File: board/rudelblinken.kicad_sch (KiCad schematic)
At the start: 0 parts

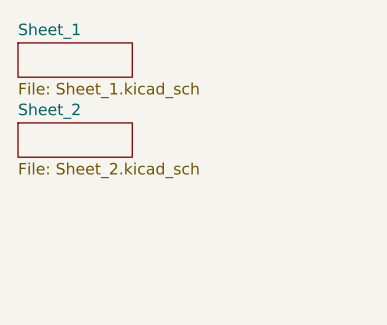
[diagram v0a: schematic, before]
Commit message: Organize schematics for kicad
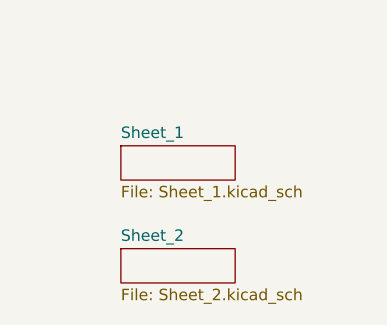
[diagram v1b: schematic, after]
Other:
- company: (none) -> Zebreus
- title: (none) -> Rudelblinken
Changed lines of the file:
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@@
 	(generator_version "8.0")
 	(paper "A4")
+	(title_block
+		(title "Rudelblinken")
+		(rev "0.1")
+		(company "Zebreus")
+	)
 	(sheet
-		(at 5.08 13.97)
+		(at 16.51 27.94)
 		(size 12.7 3.81)
 		(fields_autoplaced yes)
@@
 		)
 		(property "Sheetname" "Sheet_2"
-			(at 5.08 13.2584 0)
+			(at 16.51 27.2284 0)
 			(effects
 				(font
@@
 		)
 		(property "Sheetfile" "Sheet_2.kicad_sch"
-			(at 5.08 18.3646 0)
+			(at 16.51 32.3346 0)
 			(effects
 				(font
@@
 		)
 		(instances
-			(project "BackupProjects_lennarteichhorn_personal_1_20240922"
+			(project "rudelblinken"
 				(path "/adb641c0-c248-42eb-b32f-18abe654a1aa"
 					(page "3")
@@
 	)
 	(sheet
-		(at 5.08 5.08)
+		(at 16.51 16.51)
 		(size 12.7 3.81)
 		(fields_autoplaced yes)
@@
 		)
 		(property "Sheetname" "Sheet_1"
-			(at 5.08 4.3684 0)
+			(at 16.51 15.7984 0)
 			(effects
 				(font
@@
 		)
 		(property "Sheetfile" "Sheet_1.kicad_sch"
-			(at 5.08 9.4746 0)
+			(at 16.51 20.9046 0)
 			(effects
 				(font
@@
 		)
 		(instances
-			(project "BackupProjects_lennarteichhorn_personal_1_20240922"
+			(project "rudelblinken"
 				(path "/adb641c0-c248-42eb-b32f-18abe654a1aa"
 					(page "2")
